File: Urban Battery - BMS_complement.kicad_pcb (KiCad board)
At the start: 2 copper layers, 152.4 x 83.8 mm, 46 parts, among them J1 BMS IO, J10 E-Stop, J11 Contactor Connector, J12 Thermistor, J13 Thermistor, J14 Thermistor, J2 OLED Header, J3 CAN, J4 CAN, J5 Charge Connector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

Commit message: swapped run and charge labels, changed charge connector, renamed board
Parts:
- J5: footprint Connector_Molex:Molex_Micro-Fit_3.0_43650-0200_1x02_P3.00mm_Horizontal -> Connector_Molex:Molex_Mini-Fit_Jr_5569-02A2_2x01_P4.20mm_Horizontal
- moved J5 4.90 mm to (210.8, 120.5)
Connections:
- K1 pad 2: (no net) -> unconnected-(K1-Pad2)
- K2 pad 2: (no net) -> unconnected-(K2-Pad2)
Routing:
- net Charge: track 47.5 -> 41.3 mm
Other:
- board text added: "BMS BESTIE V2.0 SHELL ECO-MARATHON 2O23"
- board text added: "RUN OFF CHG"
- board text added: "Sarah Qadar Jeffrey Du"
- board text removed: "BMS Complement V1.0 Dec 14, 2022"
- board text removed: "CHG OFF RUN"
- board text removed: "Jeffrey Du Sarah Qadar"

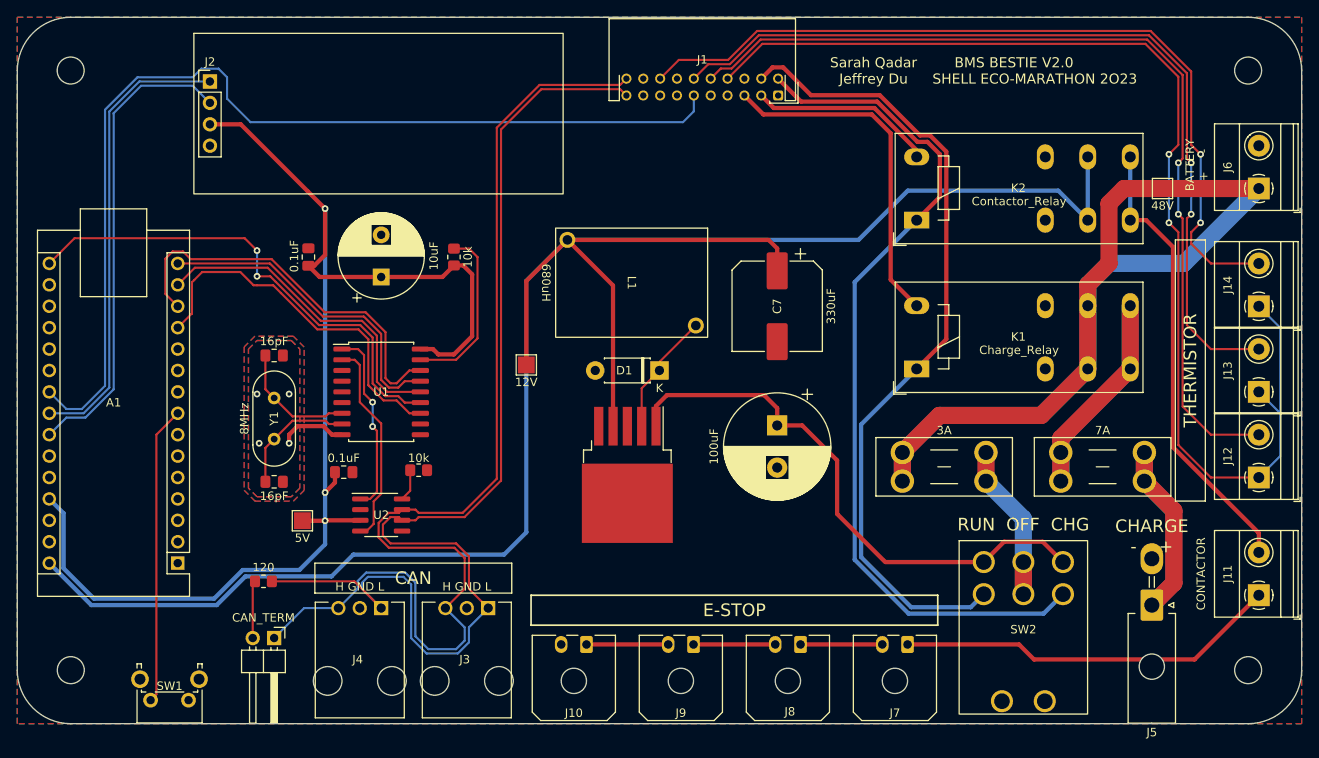
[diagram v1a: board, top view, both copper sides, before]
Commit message: added downloaded footprint for bms i/o, updated on layout. fixed orientation of charge connector labels
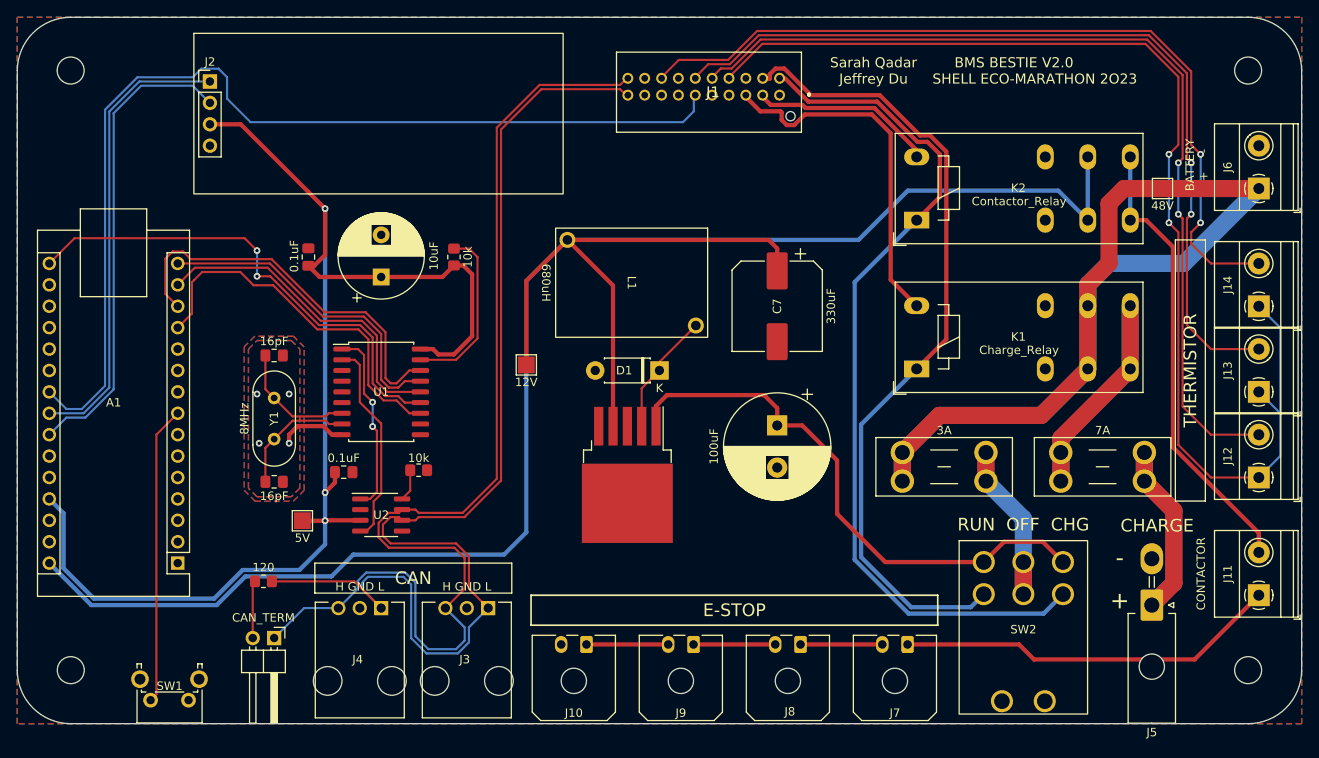
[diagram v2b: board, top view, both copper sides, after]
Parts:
- J1: footprint Connector_JST:JST_PHD_S20B-PHDSS_2x10_P2.00mm_Horizontal -> BMS_Custom_Footprints:B20BPADSS1FLFSN
- moved J1 0.17 mm to (166.7, 60.0), turned to 0 degrees
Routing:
- net bms5: track 40.9 -> 42.5 mm
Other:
- board text added: "+"
- board text added: "-"
- board text added: "CHARGE"
- board text removed: "CHARGE - +"

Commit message: fixed errors brought up by DRC on pcb
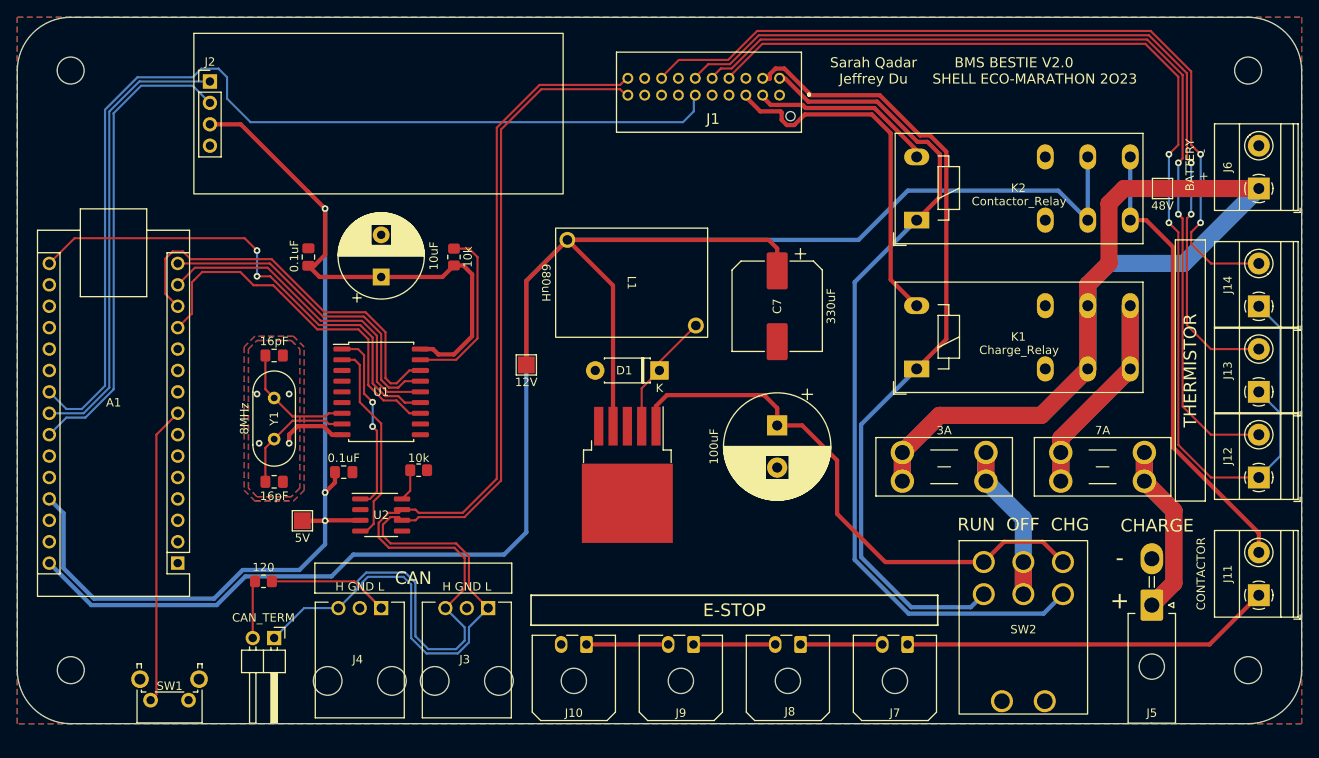
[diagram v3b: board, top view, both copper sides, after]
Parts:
- moved G*** 1.42 mm to (159.4, 71.1)
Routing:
- net Net-(J11-Pad1): track 45.6 -> 44.1 mm
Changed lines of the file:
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@@
     (property "Sheetname" "")
     (attr through_hole)
-    (fp_text reference "J5" (at 0 -15.1 180) (layer "F.SilkS")
+    (fp_text reference "J5" (at 0 -12.8 180) (layer "F.SilkS")
       (effects (font (size 1 1) (thickness 0.15)))
     )
@@
       (effects (font (size 1 1) (thickness 0.15)))
     )
-    (fp_text user "${REFERENCE}" (at 0 -13.2 180) (layer "F.Fab")
+    (fp_text user "${REFERENCE}" (at 0 -12.8 180) (layer "F.Fab")
       (effects (font (size 1 1) (thickness 0.15)))
     )
@@
     (property "Sheetname" "")
     (attr through_hole)
-    (fp_text reference "J1" (at -7.9 -0.35) (layer "F.SilkS")
+    (fp_text reference "J1" (at -7.9 2.825) (layer "F.SilkS")
       (effects (font (size 1.27 1.27) (thickness 0.254)))
     )
@@
       (effects (font (size 1.27 1.27) (thickness 0.254)))
     )
-    (fp_text user "${REFERENCE}" (at -7.9 -0.35) (layer "F.Fab")
+    (fp_text user "${REFERENCE}" (at -7.9 2.825) (layer "F.Fab")
       (effects (font (size 1.27 1.27) (thickness 0.254)))
     )
@@
   )
   (footprint "LOGO" (layer "F.Cu")
-    (at 158.75 69.85)
+    (at 159.385 71.12)
     (attr board_only exclude_from_pos_files exclude_from_bom)
     (fp_text reference "G***" (at 0 0) (layer "F.Fab")
@@
   (segment (start 209.938 105.84) (end 213.44 109.342) (width 2.032) (layer "B.Cu") (net 71))
   (segment (start 209.938 105.84) (end 209.938 102.44) (width 2.032) (layer "B.Cu") (net 71))
-  (segment (start 195.07 125.22) (end 196.85 127) (width 0.508) (layer "F.Cu") (net 72))
-  (segment (start 181.84 125.22) (end 195.07 125.22) (width 0.508) (layer "F.Cu") (net 72))
-  (segment (start 215.9 127) (end 223.52 119.38) (width 0.508) (layer "F.Cu") (net 72))
-  (segment (start 196.85 127) (end 215.9 127) (width 0.508) (layer "F.Cu") (net 72))
+  (segment (start 181.84 125.22) (end 217.68 125.22) (width 0.508) (layer "F.Cu") (net 72))
+  (segment (start 217.68 125.22) (end 223.52 119.38) (width 0.508) (layer "F.Cu") (net 72))
   (zone (net 4) (net_name "GND") (layers F&B.Cu) (hatch edge 0.508)
     (priority 1)
